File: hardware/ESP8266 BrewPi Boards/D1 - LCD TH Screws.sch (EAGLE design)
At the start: 8 parts, among them J1 RJ11-4L-B

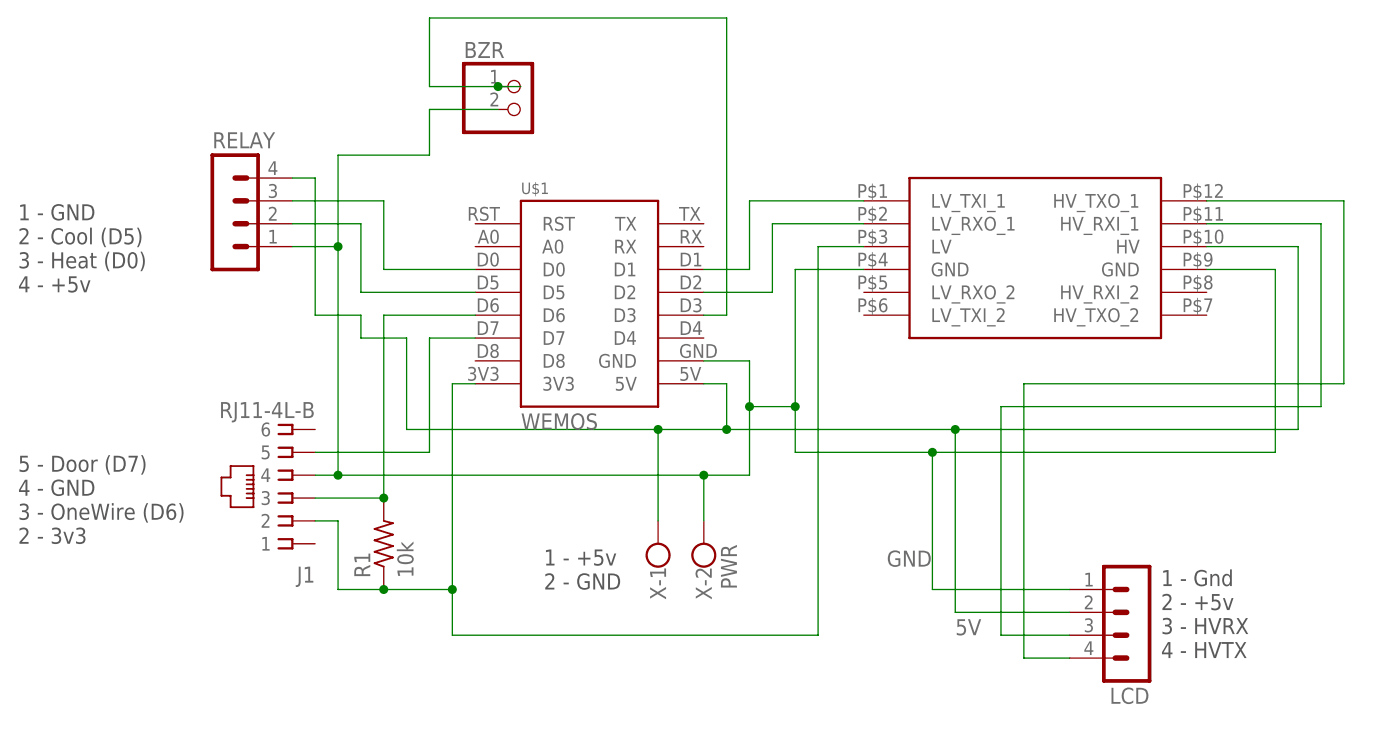
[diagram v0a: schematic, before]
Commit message: Updating docs & adding new eagle schematics
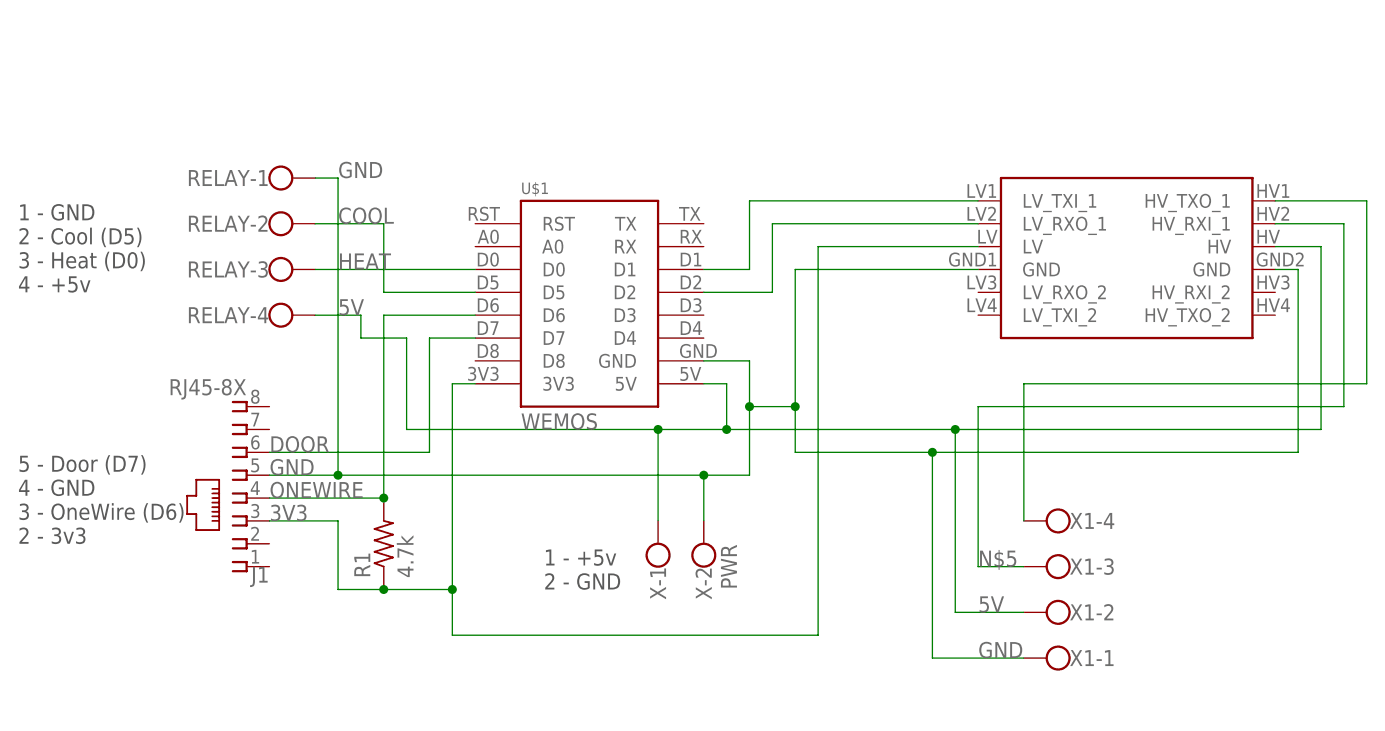
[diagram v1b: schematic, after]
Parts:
- removed BZR: (no value), pinhead:PINHD-1X2
- removed LCD: (no value), con-lstb:MA04-1
- added X1: (no value), con-wago-500:W237-4
- J1: value RJ11-4L-B -> RJ45-8X; device con-tycoelectronics:RJ11-4L-B -> con-tycoelectronics:RJ45-8X
- R1: value 10k -> 4.7k; device rcl:R-US_0207/5V -> rcl:R-US_0309/12
- RELAY: device con-lstb:MA04-1 -> con-wago-500:W237-4
- U$3: value LOGIC_LEVEL_CONVERTER -> SPARKFUN_LOGIC_LEVEL_CONVERTER; device SparkFun-Boards:LOGIC_LEVEL_CONVERTER -> SparkFun-Boards:SPARKFUN_LOGIC_LEVEL_CONVERTER
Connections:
- removed net D6: J1.3, R1.2, U$1.D6
- removed net D7: J1.5, U$1.D7
- removed net N$3: J1.2, R1.1, U$1.3V3, U$3.LV
- removed net N$6: BZR.1, U$1.D3
- removed net N$7: RELAY.2, U$1.D5
- removed net N$8: RELAY.3, U$1.D0
- new net 3V3: J1.3, R1.1, U$1.3V3, U$3.LV
- new net COOL: RELAY-2.KL, U$1.D5
- new net DOOR: J1.6, U$1.D7
- new net HEAT: RELAY-3.KL, U$1.D0
- new net ONEWIRE: J1.4, R1.2, U$1.D6
- net 5V: now also RELAY-4.KL, X1-2.KL; no longer LCD.2, RELAY.4
- net GND: now also J1.5, RELAY-1.KL, X1-1.KL; no longer BZR.2, J1.4, LCD.1, RELAY.1
- net N$4: now also X1-4.KL; no longer LCD.4
- net N$5: now also X1-3.KL; no longer LCD.3
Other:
- note removed: "1 - Gnd 2 - +5v 3 - HVRX 4 - HVTX"
